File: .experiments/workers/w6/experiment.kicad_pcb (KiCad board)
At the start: 2 copper layers, 140 x 90 mm, 39 parts, among them J1 USB_C, J2 Output, J3 Debug, Q1 FS8205A, U1 USBLC6-2SC6, U2 BQ24072, U3 HY2113-KB5B, U4 MT3608, U5 AP2112K-3.3, U6 LN61CN3302MR-G

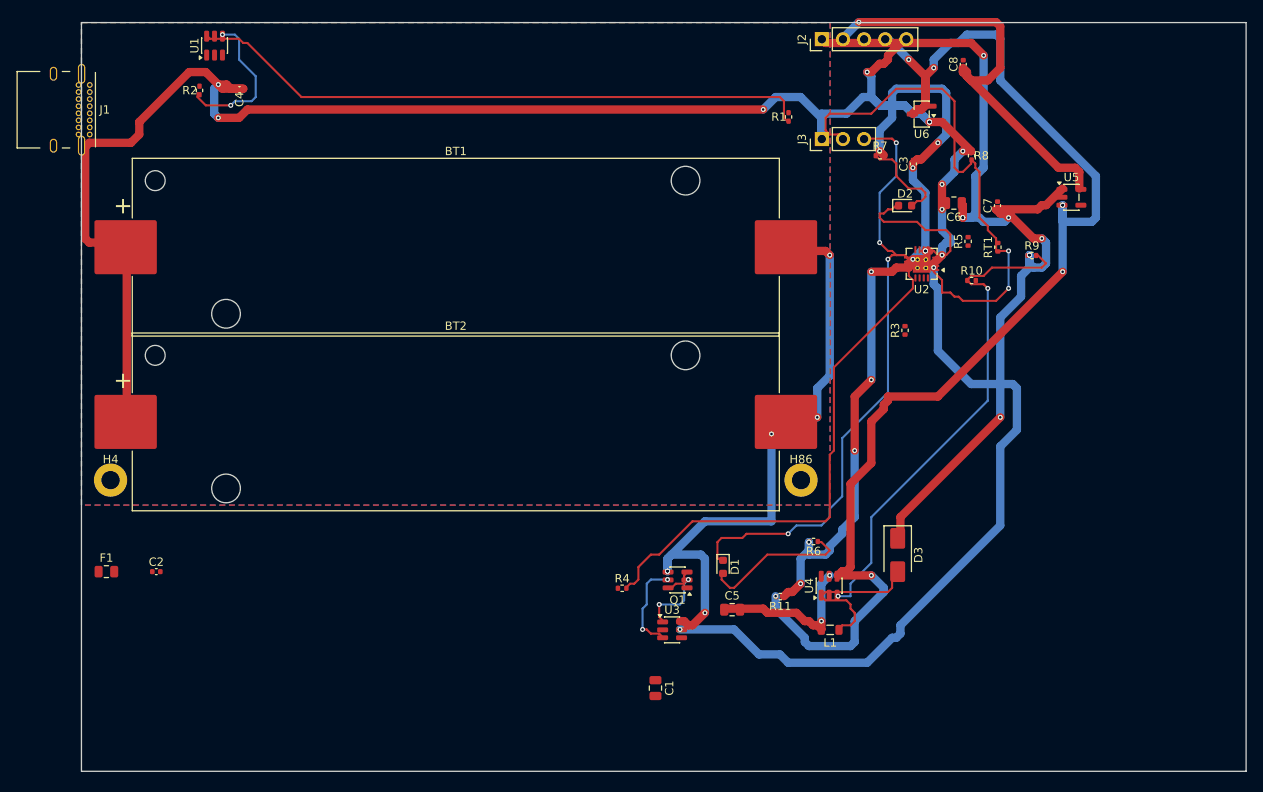
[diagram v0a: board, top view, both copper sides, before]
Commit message: 35-round experiment: best score 25.33, improved routing params
Router and conflict resolution tuning from autonomous optimization loop.
Best config: clearance=0.2051mm, cooling_factor=0.9735, existing_trace_cost=200.0

Co-Authored-By: Claude Opus 4.6 <noreply@anthropic.com>
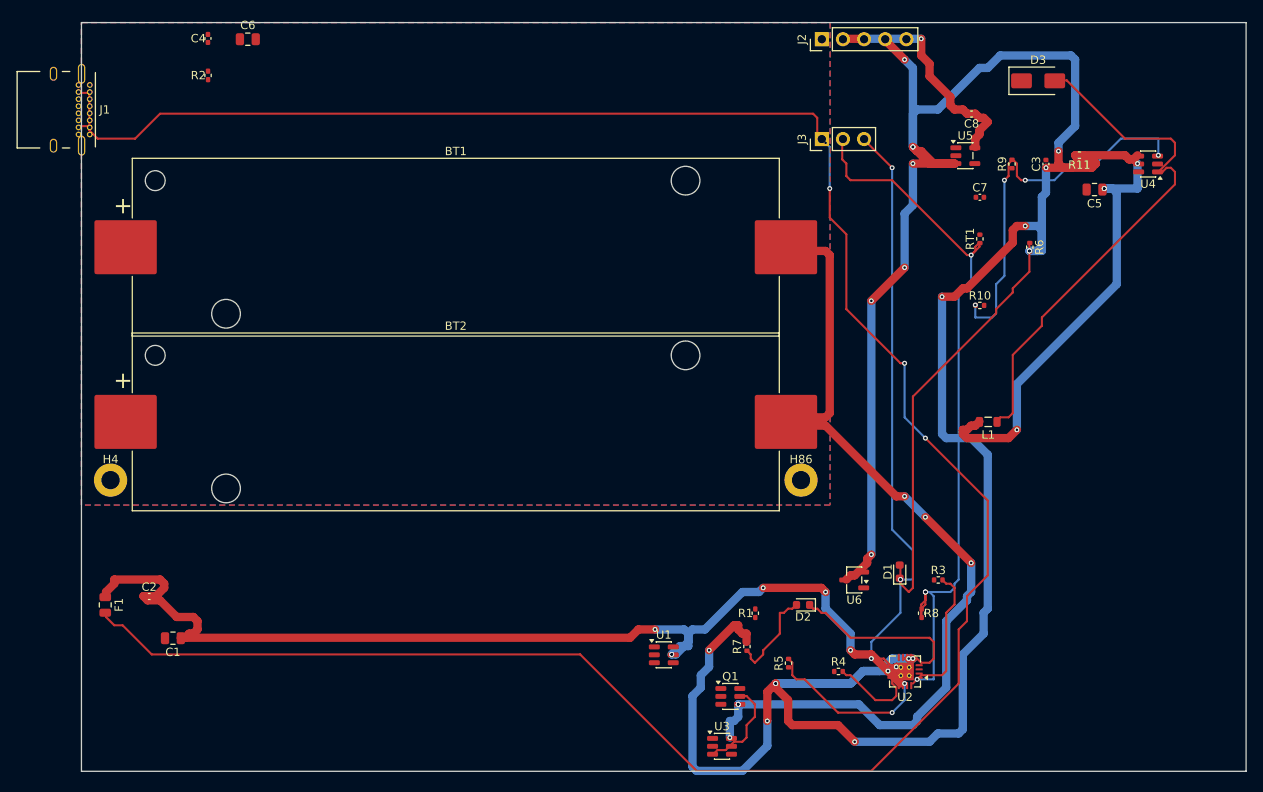
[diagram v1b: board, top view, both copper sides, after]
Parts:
- moved U1 91.0 mm to (70.0, 76.0), turned to 0 degrees
- moved C6 87.1 mm to (20.0, 2.00), turned to 0 degrees
- moved C5 66.7 mm to (121.8, 20.1), turned to 180 degrees
- moved R11 64.1 mm to (120.0, 15.9)
- moved U4 63.6 mm to (128.2, 17.0), turned to 180 degrees
- moved R7 61.1 mm to (80.0, 75.0), turned to 90 degrees
- moved R1 59.8 mm to (81.0, 71.0)
- moved D3 59.4 mm to (115.0, 7.00), turned to 0 degrees
- moved C1 58.3 mm to (11.0, 74.0), turned to 180 degrees
- moved U6 56.6 mm to (92.9, 67.0)
- moved R8 55.3 mm to (101.0, 71.0)
- moved R5 55.1 mm to (85.0, 77.0)
- moved D2 49.5 mm to (86.7, 70.0), turned to 180 degrees
- moved U2 49.0 mm to (99.0, 78.0)
- moved R6 43.9 mm to (114.0, 27.0), turned to -90 degrees
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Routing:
- net /VBAT: track 293.0 -> 0.00 mm, vias 14 -> 0
- net Net-(F1-Pad2): track 0.00 -> 289.1 mm, vias 0 -> 4
- net /VBUS: track 0.00 -> 127.2 mm, vias 0 -> 6
- net /5V: track 115.5 -> 0.00 mm, vias 8 -> 0
- net /VSYS: track 93.0 -> 198.8 mm, vias 12 -> 14
- net Net-(R1-Pad1): track 75.5 -> 0.00 mm
- net Net-(U2-ILIM): track 62.7 -> 10.4 mm
- net Net-(D3-A): track 19.7 -> 63.8 mm
- net /CELL_NEG: track 75.5 -> 109.5 mm
- net Net-(D1-A): track 17.7 -> 51.4 mm
- net /VSYS_BOOST: track 19.4 -> 52.2 mm, vias 2 -> 4
- net /NTC_SENSE: track 62.8 -> 91.6 mm, vias 2 -> 4
- net /3V3: track 52.5 -> 27.9 mm
- net Net-(U2-TMR): track 0.00 -> 20.2 mm, vias 0 -> 2
- net Net-(R2-Pad1): track 18.4 -> 0.00 mm, vias 2 -> 0
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
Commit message: 45-round experiment: best score 25.66, all nets routed (26/26)
Fixed A* performance by increasing max_search from 100k->500k to handle
high trace costs (100.0) without timing out. Kept high cost + coarse grid
(0.5mm) to prevent shorts while still routing efficiently.

Best config: edge_margin=5.7493mm, cooling_factor=0.9764, existing_trace_cost=200, max_rips=8

Co-Authored-By: Claude Opus 4.6 <noreply@anthropic.com>
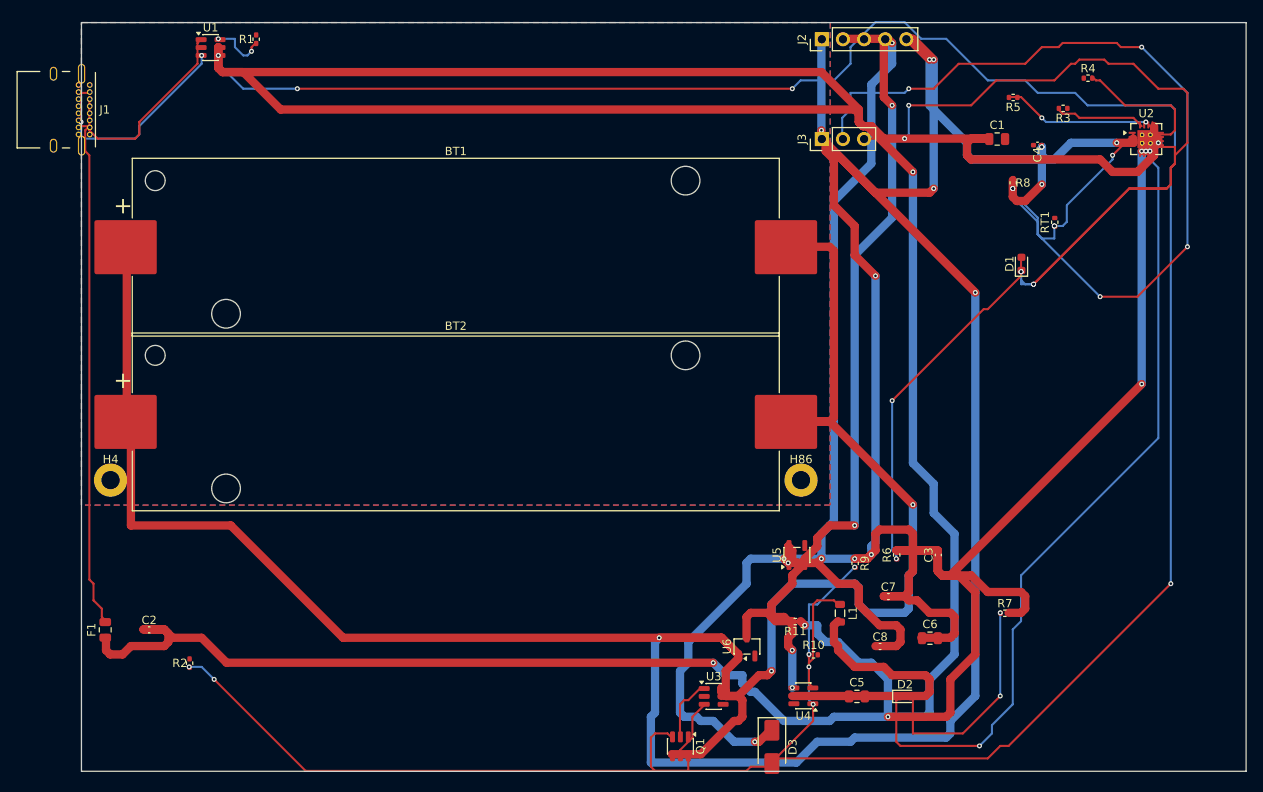
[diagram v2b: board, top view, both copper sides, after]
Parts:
- moved C1 115.8 mm to (110.1, 14.0), turned to 0 degrees
- moved C6 109.1 mm to (102.0, 74.0)
- moved C4 100.5 mm to (114.9, 14.7), turned to 180 degrees
- moved R1 91.4 mm to (21.0, 2.00)
- moved U1 91.1 mm to (15.5, 3.00)
- moved D3 86.2 mm to (83.0, 87.1), turned to -90 degrees
- moved R4 77.4 mm to (121.0, 6.68)
- moved U4 76.2 mm to (86.8, 80.9)
- moved R5 73.2 mm to (112.0, 9.00), turned to 180 degrees
- moved R2 70.7 mm to (13.0, 77.0)
- moved U2 70.3 mm to (128.0, 14.0), turned to 0 degrees
- moved C5 67.3 mm to (93.2, 81.0), turned to 0 degrees
- moved R11 65.6 mm to (85.8, 72.0)
- moved C8 64.9 mm to (96.0, 75.0), turned to 0 degrees
- moved R3 58.6 mm to (118.0, 10.3), turned to 180 degrees
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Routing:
- net /VBAT: track 0.00 -> 351.7 mm, vias 0 -> 10
- net Net-(R2-Pad1): track 0.00 -> 315.8 mm, vias 0 -> 6
- net /VBUS: track 127.2 -> 405.4 mm, vias 6 -> 2
- net Net-(F1-Pad2): track 289.1 -> 66.7 mm, vias 4 -> 0
- net /5V: track 0.00 -> 151.1 mm, vias 0 -> 8
- net /3V3: track 27.9 -> 102.0 mm
- net Net-(D2-K): track 22.8 -> 96.7 mm, vias 0 -> 2
- net /VSYS: track 198.8 -> 144.3 mm, vias 14 -> 6
- net /CHG_N: track 70.8 -> 113.8 mm, vias 4 -> 6
- net /EN: track 140.4 -> 97.4 mm, vias 8 -> 4
- net Net-(D3-A): track 63.8 -> 24.9 mm, vias 0 -> 2
- net /NTC_SENSE: track 91.6 -> 126.2 mm, vias 4 -> 10
- net Net-(U4-FB): track 47.0 -> 17.6 mm, vias 4 -> 2
- net Net-(J1-CC1): track 0.00 -> 25.2 mm
- net Net-(J1-CC2): track 0.00 -> 21.8 mm, vias 0 -> 2
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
